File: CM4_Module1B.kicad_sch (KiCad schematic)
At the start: 10 parts, among them J2 2340901-1

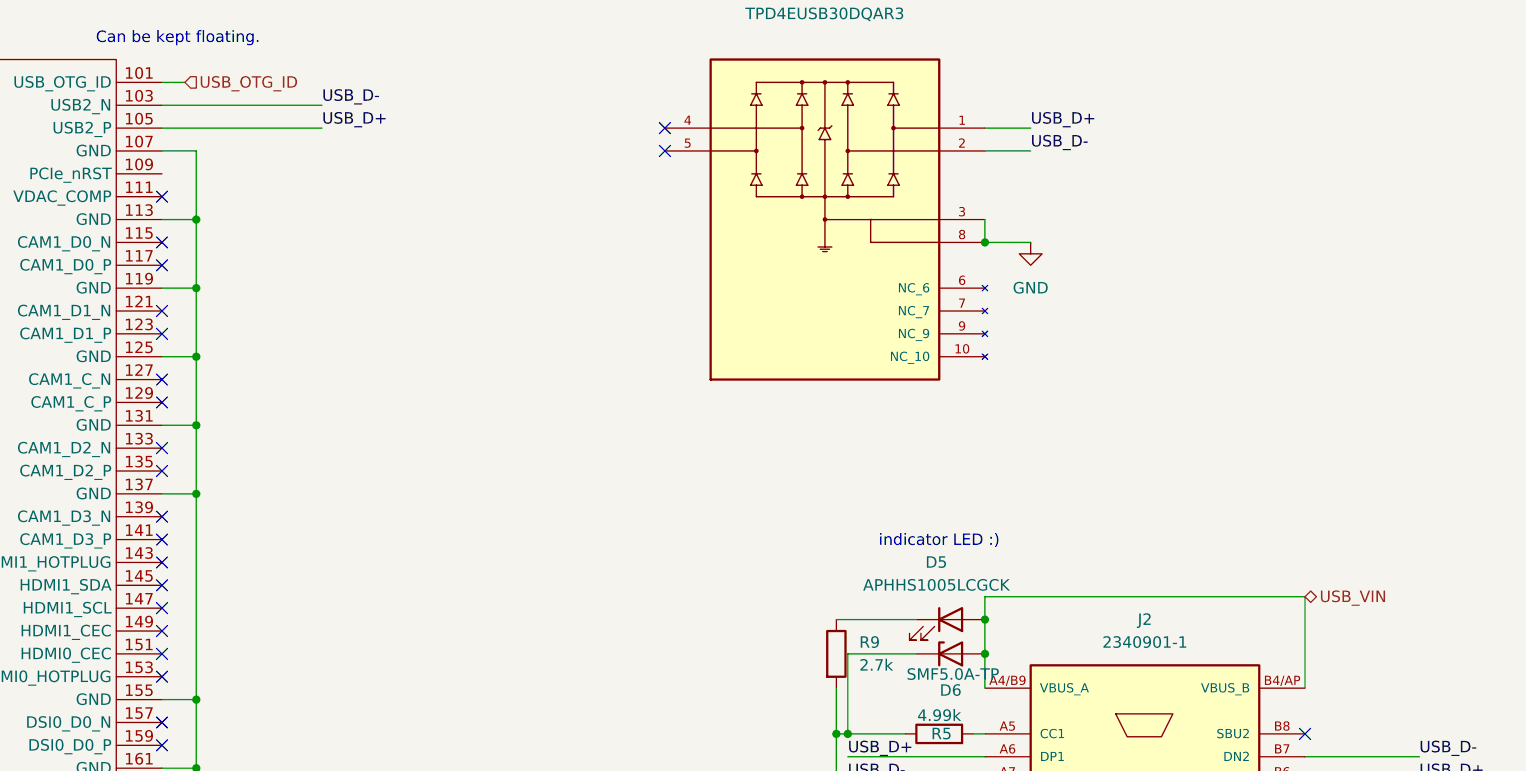
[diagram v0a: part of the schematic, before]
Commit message: added comment boxes
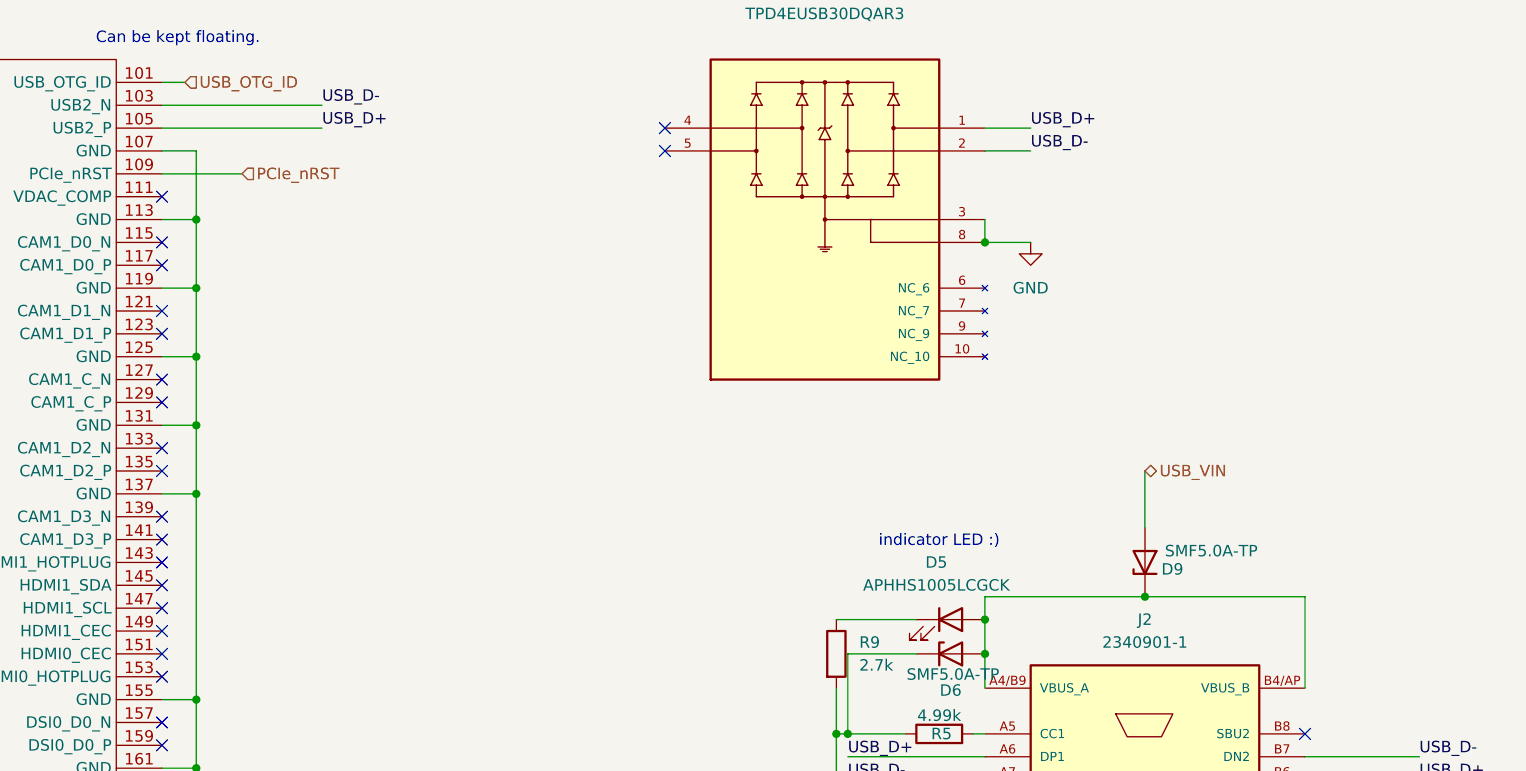
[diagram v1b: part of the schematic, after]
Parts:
- added D9: SMF5.0A-TP, dz_dio:SMF50ATP, symbol #dzdb:s_dio/D-MCC-SMF5.0A-TP
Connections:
- net USB_VIN: now also D9.2 (A); no longer D5.2 (A), D6.2 (A), J2.A4/B9 (VBUS_A), J2.B4/AP (VBUS_B)
- net PCIe_nRST: now reaches Module1.109 (PCIe_nRST)
- new net: D5.2 (A), D6.2 (A), D9.1 (K), J2.A4/B9 (VBUS_A), J2.B4/AP (VBUS_B)
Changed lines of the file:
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@@
 	)
 	(junction
+		(at 228.6 91.44)
+		(diameter 0)
+		(color 0 0 0 0)
+	)
+	(junction
 		(at 54.61 95.25)
 		(diameter 0)
@@
 	(wire
 		(pts
+			(xy 228.6 91.44) (xy 246.38 91.44)
+		)
+		(stroke
+			(width 0)
+			(type default)
+		)
+	)
+	(wire
+		(pts
 			(xy 123.19 64.77) (xy 123.19 72.39)
 		)
@@
 	(wire
 		(pts
+			(xy 119.38 44.45) (xy 128.27 44.45)
+		)
+		(stroke
+			(width 0)
+			(type default)
+		)
+	)
+	(wire
+		(pts
 			(xy 119.38 125.73) (xy 123.19 125.73)
 		)
@@
 	(wire
 		(pts
+			(xy 228.6 77.47) (xy 228.6 83.82)
+		)
+		(stroke
+			(width 0)
+			(type default)
+		)
+	)
+	(wire
+		(pts
 			(xy 123.19 57.15) (xy 123.19 64.77)
 		)
@@
 	(wire
 		(pts
-			(xy 210.82 91.44) (xy 246.38 91.44)
+			(xy 210.82 91.44) (xy 228.6 91.44)
 		)
 		(stroke
@@
 		)
 	)
-	(hierarchical_label "USB_VIN"
+	(hierarchical_label "PCIe_TX_P"
 		(shape bidirectional)
-		(at 246.38 91.44 0)
+		(at 49.53 59.69 180)
 		(effects
 			(font
 				(size 1.27 1.27)
 			)
-			(justify left)
+			(justify right)
 		)
 	)
-	(hierarchical_label "PCIe_TX_P"
+	(hierarchical_label "PCIe_CLK_P"
 		(shape bidirectional)
-		(at 49.53 59.69 180)
+		(at 49.53 44.45 180)
 		(effects
 			(font
@@
 		)
 	)
-	(hierarchical_label "PCIe_CLK_P"
-		(shape bidirectional)
-		(at 49.53 44.45 180)
+	(hierarchical_label "PCIe_nRST"
+		(shape input)
+		(at 128.27 44.45 0)
 		(effects
 			(font
 				(size 1.27 1.27)
 			)
-			(justify right)
+			(justify left)
 		)
 	)
@@
 		)
 	)
+	(hierarchical_label "USB_VIN"
+		(shape bidirectional)
+		(at 228.6 77.47 0)
+		(effects
+			(font
+				(size 1.27 1.27)
+			)
+			(justify left)
+		)
+	)
 	(hierarchical_label "PCIe_RX_N"
 		(shape bidirectional)
@@
 					(unit 1)
 				)
+			)
+		)
+	)
+	(symbol
+		(lib_id "#dzdb:s_dio/D-MCC-SMF5.0A-TP")
+		(at 228.6 87.63 90)
+		(unit 1)
+		(exclude_from_sim no)
+		(in_bom yes)
+		(on_board yes)
+		(dnp no)
+		(property "Reference" "D9"
+			(at 231.648 88.392 90)
+			(effects
+				(font
+					(size 1.27 1.27)
+				)
+			)
+		)
+		(property "Value" "SMF5.0A-TP"
+			(at 235.966 86.36 90)
+			(effects
+				(font
+					(size 1.27 1.27)
+				)
+			)
+		)
+		(property "Footprint" "dz_dio:SMF50ATP"
+			(at 228.6 87.63 0)
+			(effects
+				(font
+					(size 1.27 1.27)
+				)
+				(hide yes)
+			)
+		)
+		(property "Datasheet" "https://www.mouser.ch/datasheet/3/225/1/SMF5.0A_SMF200CA(SOD-123FL).pdf"
+			(at 228.6 87.63 0)
+			(effects
+				(font
+					(size 1.27 1.27)
+				)
+				(hide yes)
+			)
+		)
+		(property "Description" "ESD Protection Diodes / TVS Diodes TVS 200W 9.2V"
+			(at 228.6 87.63 0)
+			(effects
+				(font
+					(size 1.27 1.27)
+				)
+				(hide yes)
+			)
+		)
+		(property "IPN" "D-MCC-SMF5.0A-TP"
+			(at 228.6 87.63 0)
+			(effects
+				(font
+					(size 1.27 1.27)
+				)
+				(hide yes)
+			)
+		)
+		(property "MPN" "SMF5.0A-TP"
+			(at 228.6 87.63 0)
+			(effects
+				(font
+					(size 1.27 1.27)
+				)
+				(hide yes)
+			)
+		)
+		(property "Manufacturer" "Micro Commercial Components"
+			(at 228.6 87.63 0)
+			(effects
+				(font
+					(size 1.27 1.27)
+				)
+				(hide yes)
+			)
+		)
+		(property "Type" "Zener Diode"
+			(at 228.6 87.63 0)
+			(effects
+				(font
+					(size 1.27 1.27)
+				)
+				(hide yes)
+			)
+		)
+		(property "Vf" "5V"
+			(at 228.6 87.63 0)
+			(effects
+				(font
+					(size 1.27 1.27)
+				)
+				(hide yes)
+			)
+		)
+		(property "If" "20A"
+			(at 228.6 87.63 0)
+			(effects
+				(font
+					(size 1.27 1.27)
+				)
+				(hide yes)
+			)
+		)
+		(property "Supplier" "Mouser"
+			(at 228.6 87.63 0)
+			(effects
+				(font
+					(size 1.27 1.27)
+				)
+				(hide yes)
+			)
+		)
+		(property "SPN" "833-SMF5.0A-TP"
+			(at 228.6 87.63 0)
+			(effects
+				(font
+					(size 1.27 1.27)
+				)
+				(hide yes)
+			)
+		)
+		(property "LCSC" ""
+			(at 228.6 87.63 0)
+			(effects
+				(font
+					(size 1.27 1.27)
+				)
+				(hide yes)
+			)
+		)
+		(property "Comment" ""
+			(at 228.6 87.63 0)
+			(effects
+				(font
+					(size 1.27 1.27)
+				)
+				(hide yes)
+			)
+		)
+		(pin "1"
+		)
+		(pin "2"
+		)
+		(instances
+			(project "nautilus_mainboard"
+				(path "/ce1819b2-f280-40ed-834f-6fe4d12f809d/c2b6dac3-d6fd-4d5d-bd17-0cff91db88eb/f5b638be-e0c1-4f77-ad7d-0ded62182f5f"
+					(reference "D9")
+					(unit 1)
+				)

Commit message: simple changes
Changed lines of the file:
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@@
 	(text "Super important to not differ lengths or curve a lot with D+ and D-.\nAlso should have same hole counts (vias) and same length."
 		(exclude_from_sim no)
-		(at 193.548 21.082 0)
+		(at 193.294 23.368 0)
 		(effects
 			(font
@@
 		)
 	)
+	(text_box "ESP protection for the USB"
+		(exclude_from_sim no)
+		(at 157.48 17.78 0)
+		(size 71.12 53.34)
+		(margins 0.9525 0.9525 0.9525 0.9525)
+		(stroke
+			(width 0)
+			(type solid)
+		)
+		(fill
+			(type none)
+		)
+		(effects
+			(font
+				(size 1.27 1.27)
+			)
+			(justify left top)
+		)
+	)
+	(text_box "USB Connection for CM4"
+		(exclude_from_sim no)
+		(at 182.88 73.66 0)
+		(size 88.9 81.28)
+		(margins 0.9525 0.9525 0.9525 0.9525)
+		(stroke
+			(width 0)
+			(type solid)
+		)
+		(fill
+			(type none)
+		)
+		(effects
+			(font
+				(size 1.27 1.27)
+			)
+			(justify left top)
+		)
+	)

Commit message: Added Power logic finally. (plus some comments on further improvements)
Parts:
- renumbered C5 to C20, D9 to D7, J2 to J5, R5 to R10, R7 to R11, R6 to R12
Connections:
- net USB_VIN renamed USB_Out_5V
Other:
- note added: "Can be kept floating. if no usb is connected"
- note removed: "Can be kept floating."
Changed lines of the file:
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@@
 	(generator_version "9.0")
 	(paper "A4")
-	(text "Can be kept floating."
+	(text "Can be kept floating. if no usb is connected"
 		(exclude_from_sim no)
-		(at 121.158 29.464 0)
+		(at 130.048 28.956 0)
 		(effects
 			(font
@@
 	)
 	(junction
+		(at 228.6 77.47)
+		(diameter 0)
+		(color 0 0 0 0)
+	)
+	(junction
 		(at 123.19 125.73)
 		(diameter 0)
@@
 	(wire
 		(pts
+			(xy 224.79 77.47) (xy 228.6 77.47)
+		)
+		(stroke
+			(width 0)
+			(type default)
+		)
+	)
+	(wire
+		(pts
 			(xy 123.19 110.49) (xy 123.19 102.87)
 		)
@@
 	(wire
 		(pts
+			(xy 228.6 77.47) (xy 232.41 77.47)
+		)
+		(stroke
+			(width 0)
+			(type default)
+		)
+	)
+	(wire
+		(pts
 			(xy 54.61 49.53) (xy 54.61 57.15)
 		)
@@
 	(wire
 		(pts
-			(xy 54.61 87.63) (xy 54.61 80.01)
+			(xy 228.6 77.47) (xy 228.6 83.82)
 		)
 		(stroke
@@
 	(wire
 		(pts
-			(xy 119.38 102.87) (xy 123.19 102.87)
+			(xy 54.61 87.63) (xy 54.61 80.01)
 		)
 		(stroke
@@
 	(wire
 		(pts
-			(xy 210.82 41.91) (xy 215.9 41.91)
+			(xy 119.38 102.87) (xy 123.19 102.87)
 		)
 		(stroke
@@
 	(wire
 		(pts
-			(xy 123.19 80.01) (xy 123.19 72.39)
+			(xy 210.82 41.91) (xy 215.9 41.91)
 		)
 		(stroke
@@
 	(wire
 		(pts
-			(xy 54.61 133.35) (xy 54.61 140.97)
+			(xy 123.19 80.01) (xy 123.19 72.39)
 		)
 		(stroke
@@
 	(wire
 		(pts
-			(xy 119.38 34.29) (xy 121.92 34.29)
+			(xy 54.61 133.35) (xy 54.61 140.97)
 		)
 		(stroke
@@
 	(wire
 		(pts
-			(xy 228.6 77.47) (xy 228.6 83.82)
+			(xy 119.38 34.29) (xy 121.92 34.29)
 		)
 		(stroke
@@
 		)
 	)
+	(global_label "USB_Out_5V"
+		(shape output)
+		(at 232.41 77.47 0)
+		(fields_autoplaced yes)
+		(effects
+			(font
+				(size 1.27 1.27)
+			)
+			(justify left)
+		)
+		(property "Intersheetrefs" "${INTERSHEET_REFS}"
+			(at 246.6437 77.47 0)
+			(effects
+				(font
+					(size 1.27 1.27)
+				)
+				(justify left)
+				(hide yes)
+			)
+		)
+	)
+	(hierarchical_label "USB_OTG_5V"
+		(shape input)
+		(at 224.79 77.47 180)
+		(effects
+			(font
+				(size 1.27 1.27)
+			)
+			(justify right)
+		)
+	)
 	(hierarchical_label "PCIe_TX_P"
 		(shape bidirectional)
@@
 		)
 	)
-	(hierarchical_label "USB_VIN"
-		(shape bidirectional)
-		(at 228.6 77.47 0)
-		(effects
-			(font
-				(size 1.27 1.27)
-			)
-			(justify left)
-		)
-	)
 	(hierarchical_label "PCIe_RX_N"
 		(shape bidirectional)
@@
 		(dnp no)
 		(fields_autoplaced yes)
-		(property "Reference" "#PWR021"
+		(property "Reference" "#PWR023"
 			(at 195.58 125.73 0)
 			(effects
@@
 			(project "nautilus_mainboard"
 				(path "/ce1819b2-f280-40ed-834f-6fe4d12f809d/c2b6dac3-d6fd-4d5d-bd17-0cff91db88eb/f5b638be-e0c1-4f77-ad7d-0ded62182f5f"
-					(reference "#PWR021")
+					(reference "#PWR023")
 					(unit 1)
 				)
@@
 		(dnp no)
 		(fields_autoplaced yes)
-		(property "Reference" "J2"
+		(property "Reference" "J5"
 			(at 228.6 93.98 0)
 			(effects
@@
 			(project ""
 				(path "/ce1819b2-f280-40ed-834f-6fe4d12f809d/c2b6dac3-d6fd-4d5d-bd17-0cff91db88eb/f5b638be-e0c1-4f77-ad7d-0ded62182f5f"
-					(reference "J2")
+					(reference "J5")
 					(unit 1)
 				)
@@
 		(on_board yes)
 		(dnp no)
-		(property "Reference" "C5"
+		(property "Reference" "C20"
 			(at 205.486 135.636 90)
 			(effects
@@
 			(project ""
 				(path "/ce1819b2-f280-40ed-834f-6fe4d12f809d/c2b6dac3-d6fd-4d5d-bd17-0cff91db88eb/f5b638be-e0c1-4f77-ad7d-0ded62182f5f"
-					(reference "C5")
+					(reference "C20")
 					(unit 1)
 				)
@@
 		(dnp no)
 		(fields_autoplaced yes)
-		(property "Reference" "R7"
+		(property "Reference" "R11"
 			(at 205.74 121.92 90)
 			(effects
@@
 			(project ""
 				(path "/ce1819b2-f280-40ed-834f-6fe4d12f809d/c2b6dac3-d6fd-4d5d-bd17-0cff91db88eb/f5b638be-e0c1-4f77-ad7d-0ded62182f5f"
-					(reference "R7")
+					(reference "R11")
 					(unit 1)
 				)
@@
 		(on_board yes)
 		(dnp no)
-		(property "Reference" "R5"
+		(property "Reference" "R10"
 			(at 205.994 106.68 90)
 			(effects
@@
 			(project "nautilus_mainboard"
 				(path "/ce1819b2-f280-40ed-834f-6fe4d12f809d/c2b6dac3-d6fd-4d5d-bd17-0cff91db88eb/f5b638be-e0c1-4f77-ad7d-0ded62182f5f"
-					(reference "R5")
+					(reference "R10")
 					(unit 1)
 				)
@@
 		(on_board yes)
 		(dnp no)
-		(property "Reference" "D9"
+		(property "Reference" "D7"
 			(at 231.648 88.392 90)
 			(effects
@@
 			(project "nautilus_mainboard"
 				(path "/ce1819b2-f280-40ed-834f-6fe4d12f809d/c2b6dac3-d6fd-4d5d-bd17-0cff91db88eb/f5b638be-e0c1-4f77-ad7d-0ded62182f5f"
-					(reference "D9")
+					(reference "D7")
 					(unit 1)
 				)
@@
 		(dnp no)
 		(fields_autoplaced yes)
-		(property "Reference" "#PWR019"
+		(property "Reference" "#PWR024"
 			(at 215.9 58.42 0)
 			(effects
@@
 			(project ""
 				(path "/ce1819b2-f280-40ed-834f-6fe4d12f809d/c2b6dac3-d6fd-4d5d-bd17-0cff91db88eb/f5b638be-e0c1-4f77-ad7d-0ded62182f5f"
-					(reference "#PWR019")
+					(reference "#PWR024")
 					(unit 1)
 				)
@@
 		(dnp no)
 		(fields_autoplaced yes)
-		(property "Reference" "#PWR020"
+		(property "Reference" "#PWR025"
 			(at 259.08 125.73 0)
 			(effects
@@
 			(project ""
 				(path "/ce1819b2-f280-40ed-834f-6fe4d12f809d/c2b6dac3-d6fd-4d5d-bd17-0cff91db88eb/f5b638be-e0c1-4f77-ad7d-0ded62182f5f"
-					(reference "#PWR020")
+					(reference "#PWR025")
 					(unit 1)
 				)
@@
 		(on_board yes)
 		(dnp no)
-		(property "Reference" "R6"
+		(property "Reference" "R12"
 			(at 252.73 114.3 90)
 			(effects
@@
 			(project ""
 				(path "/ce1819b2-f280-40ed-834f-6fe4d12f809d/c2b6dac3-d6fd-4d5d-bd17-0cff91db88eb/f5b638be-e0c1-4f77-ad7d-0ded62182f5f"
-					(reference "R6")
+					(reference "R12")
 					(unit 1)
 				)
@@
 		(dnp no)
 		(fields_autoplaced yes)
-		(property "Reference" "#PWR07"
+		(property "Reference" "#PWR021"
 			(at 54.61 170.18 0)
 			(effects
@@
 			(project "nautilus_mainboard"
 				(path "/ce1819b2-f280-40ed-834f-6fe4d12f809d/c2b6dac3-d6fd-4d5d-bd17-0cff91db88eb/f5b638be-e0c1-4f77-ad7d-0ded62182f5f"
-					(reference "#PWR07")
+					(reference "#PWR021")
 					(unit 1)
 				)
@@
 		(dnp no)
 		(fields_autoplaced yes)
-		(property "Reference" "#PWR08"
+		(property "Reference" "#PWR022"
 			(at 123.19 170.18 0)
 			(effects
@@
 			(project "nautilus_mainboard"
 				(path "/ce1819b2-f280-40ed-834f-6fe4d12f809d/c2b6dac3-d6fd-4d5d-bd17-0cff91db88eb/f5b638be-e0c1-4f77-ad7d-0ded62182f5f"
-					(reference "#PWR08")
+					(reference "#PWR022")
 					(unit 1)
 				)
